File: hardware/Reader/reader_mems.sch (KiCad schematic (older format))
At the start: 3 parts

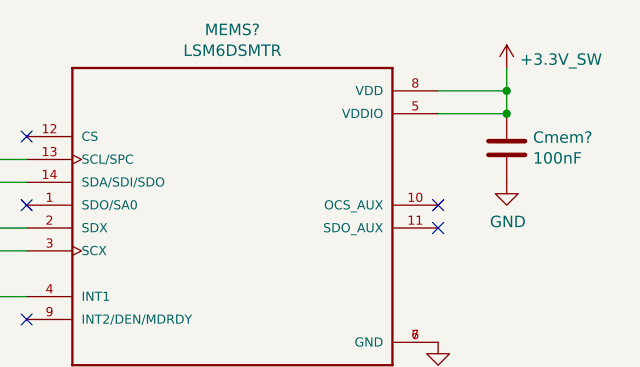
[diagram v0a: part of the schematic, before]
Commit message: Completed schematics for reader
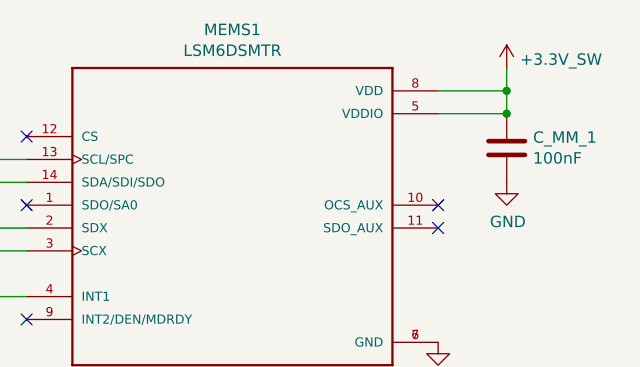
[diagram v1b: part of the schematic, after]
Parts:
- removed PWR?: +3.3V_SW, symbol CANtech:+3.3V_SW
- C_MM_1: renamed from Cmem?; footprint (none) -> footprints:FA16C0G2A104JRU06
- MEMS1: renamed from MEMS?; footprint PQFN50P300X250X86-14N -> footprints:PQFN50P300X250X86-14N
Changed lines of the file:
@@
 $Descr USLetter 11000 8500
 encoding utf-8
-Sheet 2 9
-Title ""
-Date "2020-10-18"
+Sheet 8 17
+Title "CANnect Reader | MEMs"
+Date "2020-10-20"
 Rev "0.0.1"
 Comp "CANtech"
-Comment1 ""
+Comment1 "Created by Choong Jin Ng | jin8383@gmail.com"
 Comment2 ""
 Comment3 ""
-Comment4 ""
+Comment4 "Component Identifier: MM"
 $EndDescr
 $Comp
@@
 P 6550 3400
 AR Path="/5F9A440D" Ref="MEMS?"  Part="1"
-AR Path="/5F988046/5F9A440D" Ref="MEMS?"  Part="1"
-F 0 "MEMS?" H 6550 4167 50  0000 C CNN
+AR Path="/5F988046/5F9A440D" Ref="MEMS1"  Part="1"
+F 0 "MEMS1" H 6550 4167 50  0000 C CNN
 F 1 "LSM6DSMTR" H 6550 4076 50  0000 C CNN
-F 2 "PQFN50P300X250X86-14N" H 6550 3400 50  0001 L BNN
+F 2 "footprints:PQFN50P300X250X86-14N" H 6550 3400 50  0001 L BNN
 F 3 "STMicroelectronics" H 6550 3400 50  0001 L BNN
 F 4 "0.86 mm" H 6550 3400 50  0001 L BNN "Field4"
@@
 P 7750 3150
 AR Path="/5F9A441F" Ref="Cmem?"  Part="1"
-AR Path="/5F988046/5F9A441F" Ref="Cmem?"  Part="1"
-F 0 "Cmem?" H 7865 3196 50  0000 L CNN
+AR Path="/5F988046/5F9A441F" Ref="C_MM_1"  Part="1"
+F 0 "C_MM_1" H 7865 3196 50  0000 L CNN
 F 1 "100nF" H 7865 3105 50  0000 L CNN
-F 2 "" H 7788 3000 50  0001 C CNN
-F 3 "~" H 7750 3150 50  0001 C CNN
+F 2 "footprints:FA16C0G2A104JRU06" H 7788 3000 50  0001 C CNN
+F 3 "https://product.tdk.com/info/en/catalog/datasheets/leadmlcc_halogenfree_fa_en.pdf" H 7750 3150 50  0001 C CNN
 	1    7750 3150
 	1    0    0    -1
@@
 NoConn ~ 5650 3100
 $Comp
-L CANtech:+3.3V_SW PWR?
+L CANtech:+3.3V_SW #PWR0143
 U 1 1 5FA73E29
 P 7750 2800
-F 0 "PWR?" H 7750 3050 50  0001 C CNN
+F 0 "#PWR0143" H 7750 3050 50  0001 C CNN
 F 1 "+3.3V_SW" H 7808 2837 50  0000 L CNN
 F 2 "" H 7000 3600 50  0001 C CNN

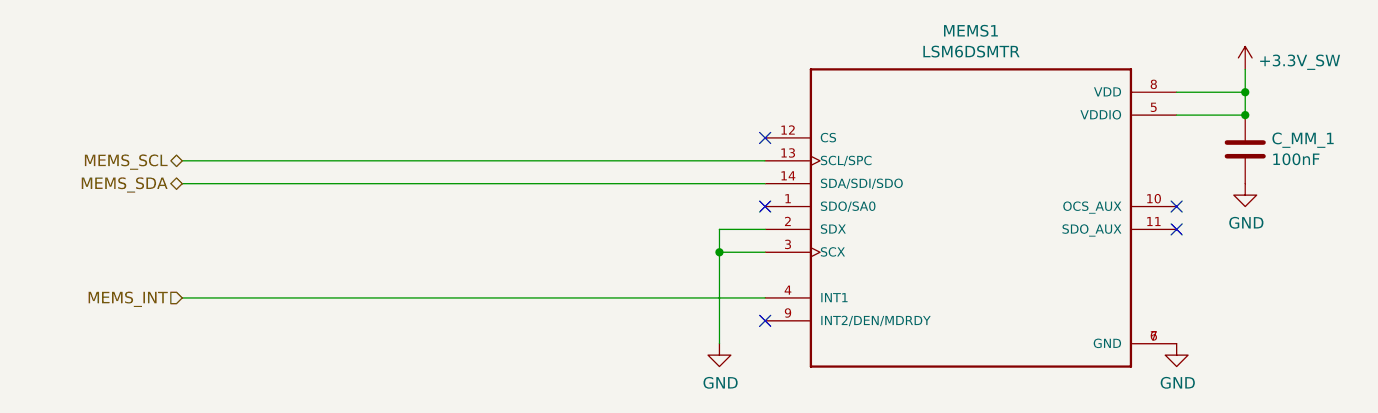
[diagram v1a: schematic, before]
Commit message: Completed Reader schematics for version 0.0.01
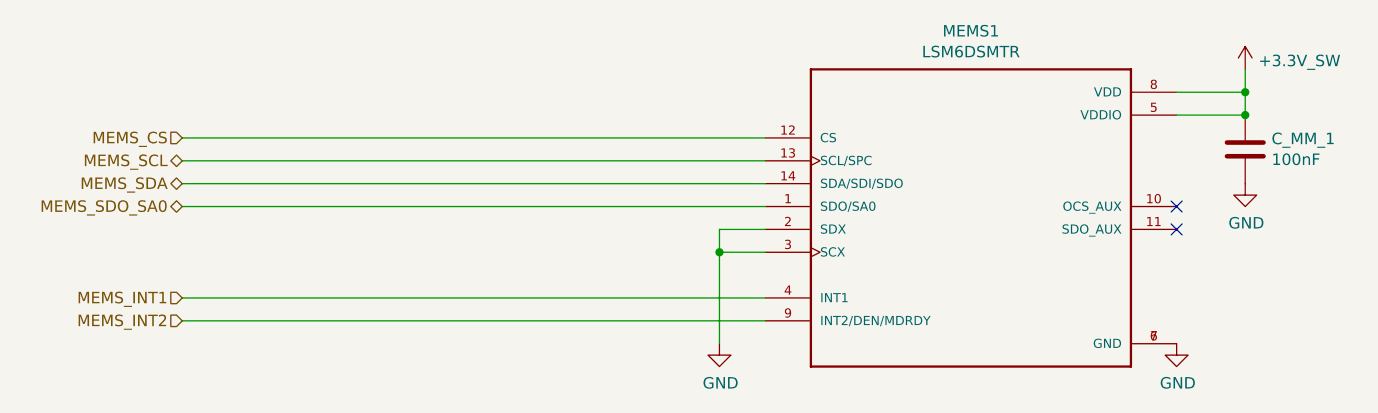
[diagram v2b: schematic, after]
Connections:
- net MEMS_SDO_SA0: now reaches MEMS1.1 (SDO/SA0)
- net MEMS_CS: now reaches MEMS1.12 (CS)
- net MEMS_INT2: now reaches MEMS1.9 (INT2/DEN/MDRDY)
- net MEMS_INT renamed MEMS_INT1
- no-connect marks 5 -> 2
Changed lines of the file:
@@
 $Descr USLetter 11000 8500
 encoding utf-8
-Sheet 8 17
+Sheet 18 18
 Title "CANnect Reader | MEMs"
 Date "2020-10-20"
-Rev "0.0.1"
+Rev "0.0.01"
 Comp "CANtech"
 Comment1 "Created by Choong Jin Ng | jin8383@gmail.com"
@@
 NoConn ~ 7450 3400
 NoConn ~ 7450 3500
-NoConn ~ 5650 3400
-NoConn ~ 5650 3900
 Text HLabel 3100 3200 0    50   BiDi ~ 0
 MEMS_SCL
@@
 MEMS_SDA
 Text HLabel 3100 3800 0    50   Input ~ 0
-MEMS_INT
+MEMS_INT1
 Wire Wire Line
 	3100 3800 5650 3800
@@
 Wire Wire Line
 	3100 3200 5650 3200
-NoConn ~ 5650 3100
 $Comp
 L CANtech:+3.3V_SW #PWR0143
@@
 	1    0    0    -1
 $EndComp
+Wire Wire Line
+	5650 3400 3100 3400
+Wire Wire Line
+	5650 3100 3100 3100
+Text HLabel 3100 3100 0    50   Input ~ 0
+MEMS_CS
+Text HLabel 3100 3400 0    50   BiDi ~ 0
+MEMS_SDO_SA0
+Text HLabel 3100 3900 0    50   Input ~ 0
+MEMS_INT2
+Wire Wire Line
+	3100 3900 5650 3900
 $EndSCHEMATC

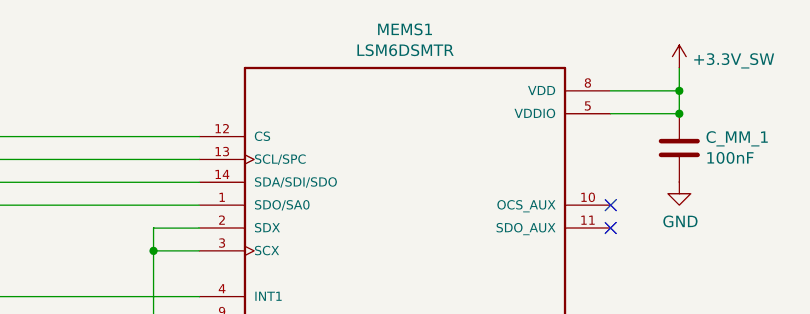
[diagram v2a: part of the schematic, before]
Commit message: Added ESD Protection. Fixed minor bugs on schematic. Attempted placement of components
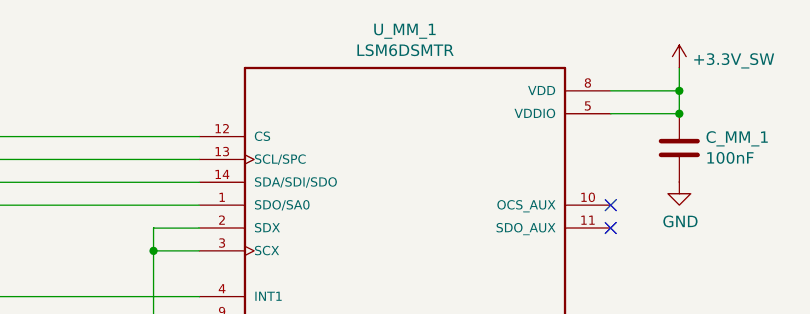
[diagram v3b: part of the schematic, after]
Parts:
- renumbered MEMS1 to U_MM_1
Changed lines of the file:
@@
 $Descr USLetter 11000 8500
 encoding utf-8
-Sheet 18 18
+Sheet 14 19
 Title "CANnect Reader | MEMs"
-Date "2020-10-20"
-Rev "0.0.01"
+Date "2020-10-25"
+Rev "0.0.03"
 Comp "CANtech"
 Comment1 "Created by Choong Jin Ng | jin8383@gmail.com"
@@
 P 6550 3400
 AR Path="/5F9A440D" Ref="MEMS?"  Part="1"
-AR Path="/5F988046/5F9A440D" Ref="MEMS1"  Part="1"
-F 0 "MEMS1" H 6550 4167 50  0000 C CNN
+AR Path="/5F988046/5F9A440D" Ref="U_MM_1"  Part="1"
+F 0 "U_MM_1" H 6550 4167 50  0000 C CNN
 F 1 "LSM6DSMTR" H 6550 4076 50  0000 C CNN
 F 2 "footprints:PQFN50P300X250X86-14N" H 6550 3400 50  0001 L BNN

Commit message: Fixed bugs on the reader schematic. Exported Schematic Electrical report
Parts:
- C_MM_1: Manufacturer (none) -> TDK Corporation; Part Name (none) -> C1608X7R2A103K080AA; Vendor (none) -> DigiKey Canada; digikeypn (none) -> 445-1304-1-ND
- U_MM_1: Manufacturer (none) -> STMicroelectronics; Part Name (none) -> LSM6DSMTR; Vendor (none) -> DigiKey Canada; digikeypn (none) -> 497-16696-1-ND
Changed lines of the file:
@@
 F 1 "LSM6DSMTR" H 6550 4076 50  0000 C CNN
 F 2 "footprints:PQFN50P300X250X86-14N" H 6550 3400 50  0001 L BNN
-F 3 "STMicroelectronics" H 6550 3400 50  0001 L BNN
+F 3 "https://www.st.com/content/ccc/resource/technical/document/datasheet/76/27/cf/88/c5/03/42/6b/DM00218116.pdf/files/DM00218116.pdf/jcr:content/translations/en.DM00218116.pdf" H 6550 3400 50  0001 L BNN
 F 4 "0.86 mm" H 6550 3400 50  0001 L BNN "Field4"
 F 5 "Rev 7" H 6550 3400 50  0001 L BNN "Field5"
 F 6 "IPC 7351B" H 6550 3400 50  0001 L BNN "Field6"
+F 7 "LSM6DSMTR" H 6550 3400 50  0001 C CNN "Part Name"
+F 8 "STMicroelectronics" H 6550 3400 50  0001 C CNN "Manufacturer"
+F 9 "DigiKey Canada" H 6550 3400 50  0001 C CNN "Vendor"
+F 10 "497-16696-1-ND" H 6550 3400 50  0001 C CNN "digikeypn"
 	1    6550 3400
 	1    0    0    -1
@@
 F 2 "footprints:FA16C0G2A104JRU06" H 7788 3000 50  0001 C CNN
 F 3 "https://product.tdk.com/info/en/catalog/datasheets/leadmlcc_halogenfree_fa_en.pdf" H 7750 3150 50  0001 C CNN
+F 4 "C1608X7R2A103K080AA" H 7750 3150 50  0001 C CNN "Part Name"
+F 5 "DigiKey Canada" H 7750 3150 50  0001 C CNN "Vendor"
+F 6 "TDK Corporation" H 7750 3150 50  0001 C CNN "Manufacturer"
+F 7 "445-1304-1-ND" H 7750 3150 50  0001 C CNN "digikeypn"
 	1    7750 3150
 	1    0    0    -1

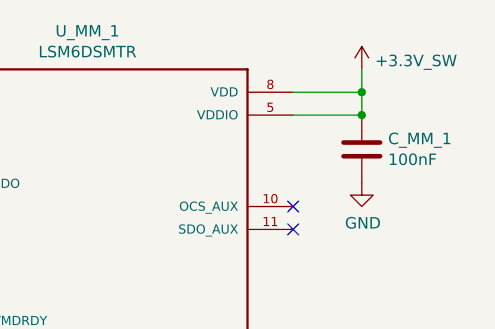
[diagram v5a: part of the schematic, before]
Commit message: Fixed minor bugs in schematic. Completed PCB layout v0.0.1 and exported Gerber files
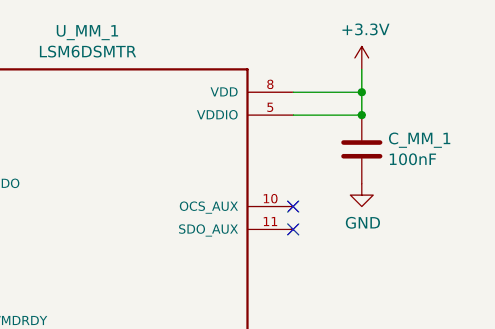
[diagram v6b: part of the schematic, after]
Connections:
- net +3.3V_SW renamed +3V3
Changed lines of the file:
@@
 Sheet 14 19
 Title "CANnect Reader | MEMs"
-Date "2020-10-25"
+Date "2020-10-27"
 Rev "0.0.03"
 Comp "CANtech"
@@
 	7450 2900 7750 2900
 Wire Wire Line
-	7750 2900 7750 2800
-Wire Wire Line
 	7450 3000 7750 3000
 Wire Wire Line
 	7750 2900 7750 3000
-Connection ~ 7750 2900
 Connection ~ 7750 3000
 NoConn ~ 7450 3400
@@
 Wire Wire Line
 	3100 3200 5650 3200
-$Comp
-L CANtech:+3.3V_SW #PWR089
-U 1 1 5FA73E29
-P 7750 2800
-F 0 "#PWR089" H 7750 3050 50  0001 C CNN
-F 1 "+3.3V_SW" H 7808 2837 50  0000 L CNN
-F 2 "" H 7000 3600 50  0001 C CNN
-F 3 "" H 7000 3600 50  0001 C CNN
-	1    7750 2800
-	1    0    0    -1
-$EndComp
 Wire Wire Line
 	5650 3400 3100 3400
@@
 Wire Wire Line
 	3100 3900 5650 3900
+Connection ~ 7750 2900
+Wire Wire Line
+	7750 2900 7750 2800
+$Comp
+L power:+3.3V #PWR089
+U 1 1 5FC85156
+P 7750 2800
+F 0 "#PWR089" H 7750 2650 50  0001 C CNN
+F 1 "+3.3V" H 7765 2973 50  0000 C CNN
+F 2 "" H 7750 2800 50  0001 C CNN
+F 3 "" H 7750 2800 50  0001 C CNN
+	1    7750 2800
+	1    0    0    -1
+$EndComp
 $EndSCHEMATC
